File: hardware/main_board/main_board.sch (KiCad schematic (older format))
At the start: 0 parts

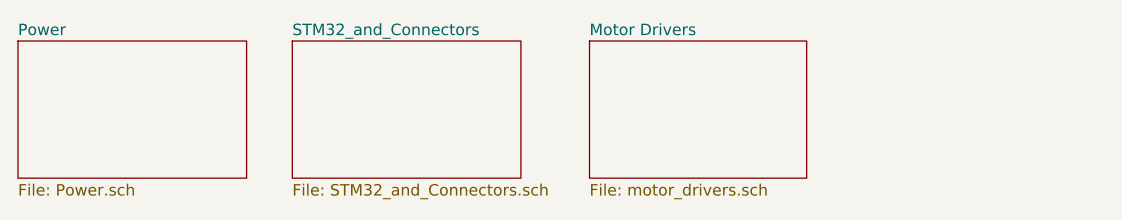
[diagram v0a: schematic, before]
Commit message: Added skittle_pnp symbol and footprint library
Added 10uF tantalum capacitor and diode to the
skittle_pnp symbol and footprints libraries.
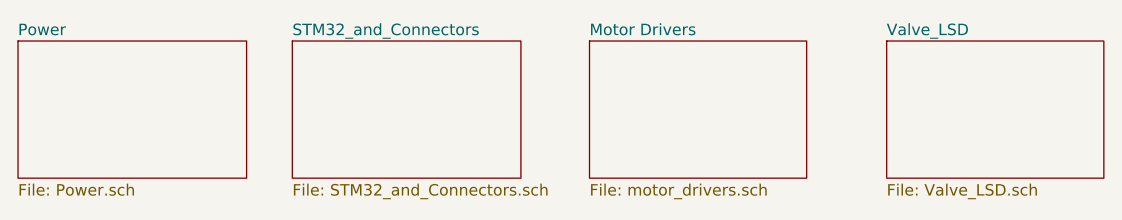
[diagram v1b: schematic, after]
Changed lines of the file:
@@
 $Descr A4 11693 8268
 encoding utf-8
-Sheet 1 4
+Sheet 1 5
 Title ""
 Date ""
@@
 F1 "STM32_and_Connectors.sch" 50
 $EndSheet
+$Sheet
+S 7250 2350 950  600
+U 6286C9DB
+F0 "Valve_LSD" 50
+F1 "Valve_LSD.sch" 50
+$EndSheet
 $EndSCHEMATC
